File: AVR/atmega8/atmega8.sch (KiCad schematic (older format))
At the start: 7 parts

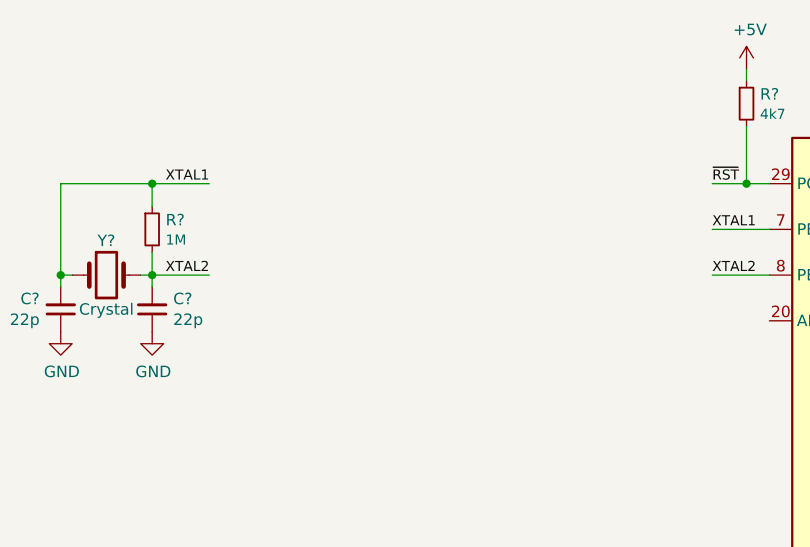
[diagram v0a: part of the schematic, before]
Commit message: Improving AVR templates
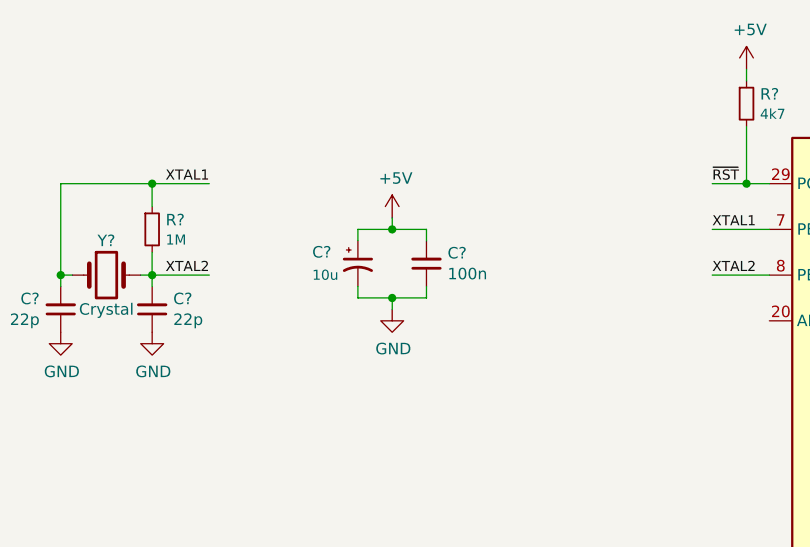
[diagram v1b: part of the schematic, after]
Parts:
- added C?: 100n, symbol Device:C_Small
- added C?: 10u, symbol Device:CP1_Small
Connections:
- net +5V: now also C?.1, C?.2
- net GND: now also C?.1, C?.2
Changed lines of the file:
@@
 EESchema Schematic File Version 4
-LIBS:XTAL-cache
-LIBS:ISP-cache
+LIBS:atmega8-cache
 EELAYER 26 0
 EELAYER END
@@
 Wire Wire Line
 	2300 5700 2300 5900
+$Comp
+L Device:C_Small C?
+U 1 1 5B85D8FB
+P 3300 2900
+F 0 "C?" H 3208 2854 50  0000 R CNN
+F 1 "100n" H 3208 2945 50  0000 R CNN
+F 2 "" H 3300 2900 50  0001 C CNN
+F 3 "~" H 3300 2900 50  0001 C CNN
+	1    3300 2900
+	-1   0    0    1
+$EndComp
+$Comp
+L power:GND #PWR?
+U 1 1 5B85D92C
+P 3150 3100
+F 0 "#PWR?" H 3150 2850 50  0001 C CNN
+F 1 "GND" H 3155 2927 50  0000 C CNN
+F 2 "" H 3150 3100 50  0001 C CNN
+F 3 "" H 3150 3100 50  0001 C CNN
+	1    3150 3100
+	1    0    0    -1
+$EndComp
+$Comp
+L power:+5V #PWR?
+U 1 1 5B85DA3C
+P 3150 2700
+F 0 "#PWR?" H 3150 2550 50  0001 C CNN
+F 1 "+5V" H 3165 2873 50  0000 C CNN
+F 2 "" H 3150 2700 50  0001 C CNN
+F 3 "" H 3150 2700 50  0001 C CNN
+	1    3150 2700
+	1    0    0    -1
+$EndComp
+$Comp
+L Device:CP1_Small C?
+U 1 1 5B85DA76
+P 3000 2900
+F 0 "C?" H 2800 2950 50  0000 L CNN
+F 1 "10u" H 2800 2850 44  0000 L CNN
+F 2 "" H 3000 2900 50  0001 C CNN
+F 3 "~" H 3000 2900 50  0001 C CNN
+	1    3000 2900
+	1    0    0    -1
+$EndComp
+Wire Wire Line
+	3000 2800 3000 2750
+Wire Wire Line
+	3000 2750 3150 2750
+Wire Wire Line
+	3300 2750 3300 2800
+Wire Wire Line
+	3000 3000 3000 3050
+Wire Wire Line
+	3000 3050 3150 3050
+Wire Wire Line
+	3300 3050 3300 3000
+Wire Wire Line
+	3150 3050 3150 3100
+Connection ~ 3150 3050
+Wire Wire Line
+	3150 3050 3300 3050
+Wire Wire Line
+	3150 2750 3150 2700
+Connection ~ 3150 2750
+Wire Wire Line
+	3150 2750 3300 2750
 $EndSCHEMATC

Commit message: Update to KiCad 5.1.7
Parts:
- U?: symbol MCU_Microchip_ATmega:ATmega8-16AU -> atmega8-rescue:ATmega8-16AU-MCU_Microchip_ATmega
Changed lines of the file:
@@
 EESchema Schematic File Version 4
-LIBS:atmega8-cache
-EELAYER 26 0
+EELAYER 30 0
 EELAYER END
 $Descr A4 11693 8268
@@
 $EndComp
 $Comp
-L MCU_Microchip_ATmega:ATmega8-16AU U?
+L atmega8-rescue:ATmega8-16AU-MCU_Microchip_ATmega U?
 U 1 1 5B83C624
 P 5400 3750
